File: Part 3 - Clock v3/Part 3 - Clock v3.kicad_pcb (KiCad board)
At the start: 2 copper layers, 100 x 100 mm, 88 parts, among them J1 BUS 1, J2 RST/CLK TP, J3 AUX PWR, SW1 RESET, SW2 MODE, SW3 SPEED, SW4 STEP, SW5 BOOT SPEED, SW6 BOOT MODE, SW7 SW_DIP_x08, SW8 RESET FAST LSB, SW9 RESET FAST MSB, U1 74AHC14, U10 74HC112, U11 74AHC74, U12 LMC555, U13 74HC251, U14 74HC40103, U15 74AHC138, U16 74HC251, U17 74HC251, U2 74AHC174, U3 74AHC08, U4 74AHC14, U5 74AHC74, U6 74AHC74, U7 74AHC74, U8 74AHC74, U9 74HC112, X1 14.7456MHz

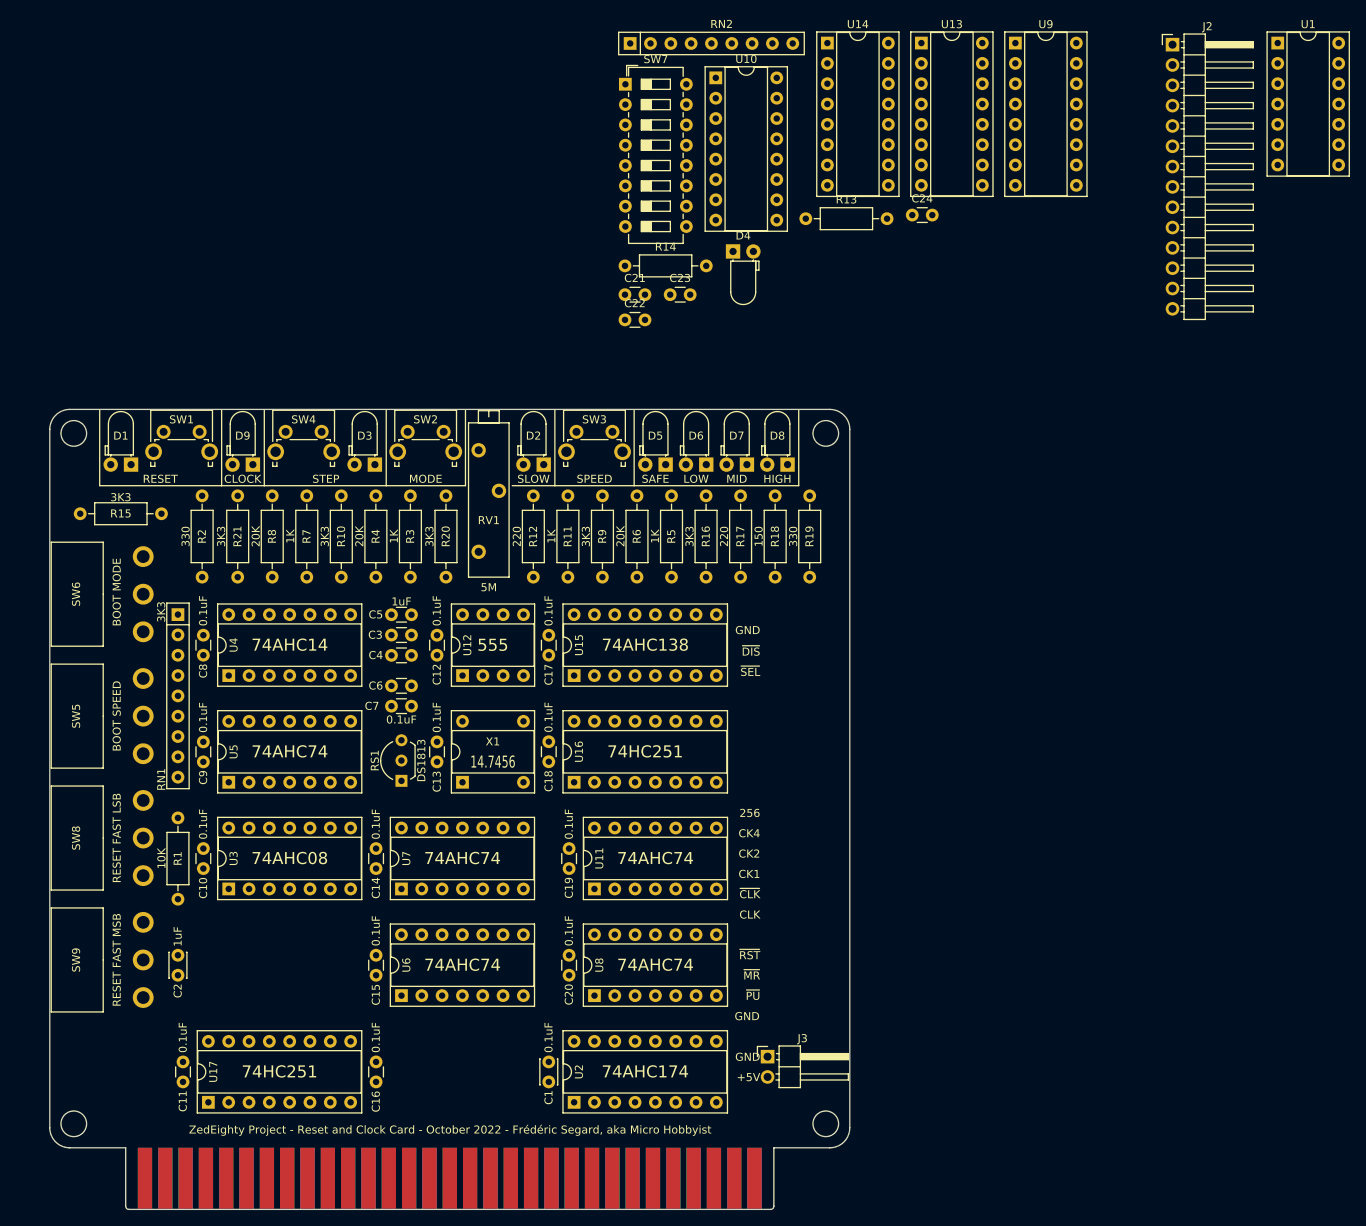
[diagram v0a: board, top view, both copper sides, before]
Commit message: Attempted to reduce chip count
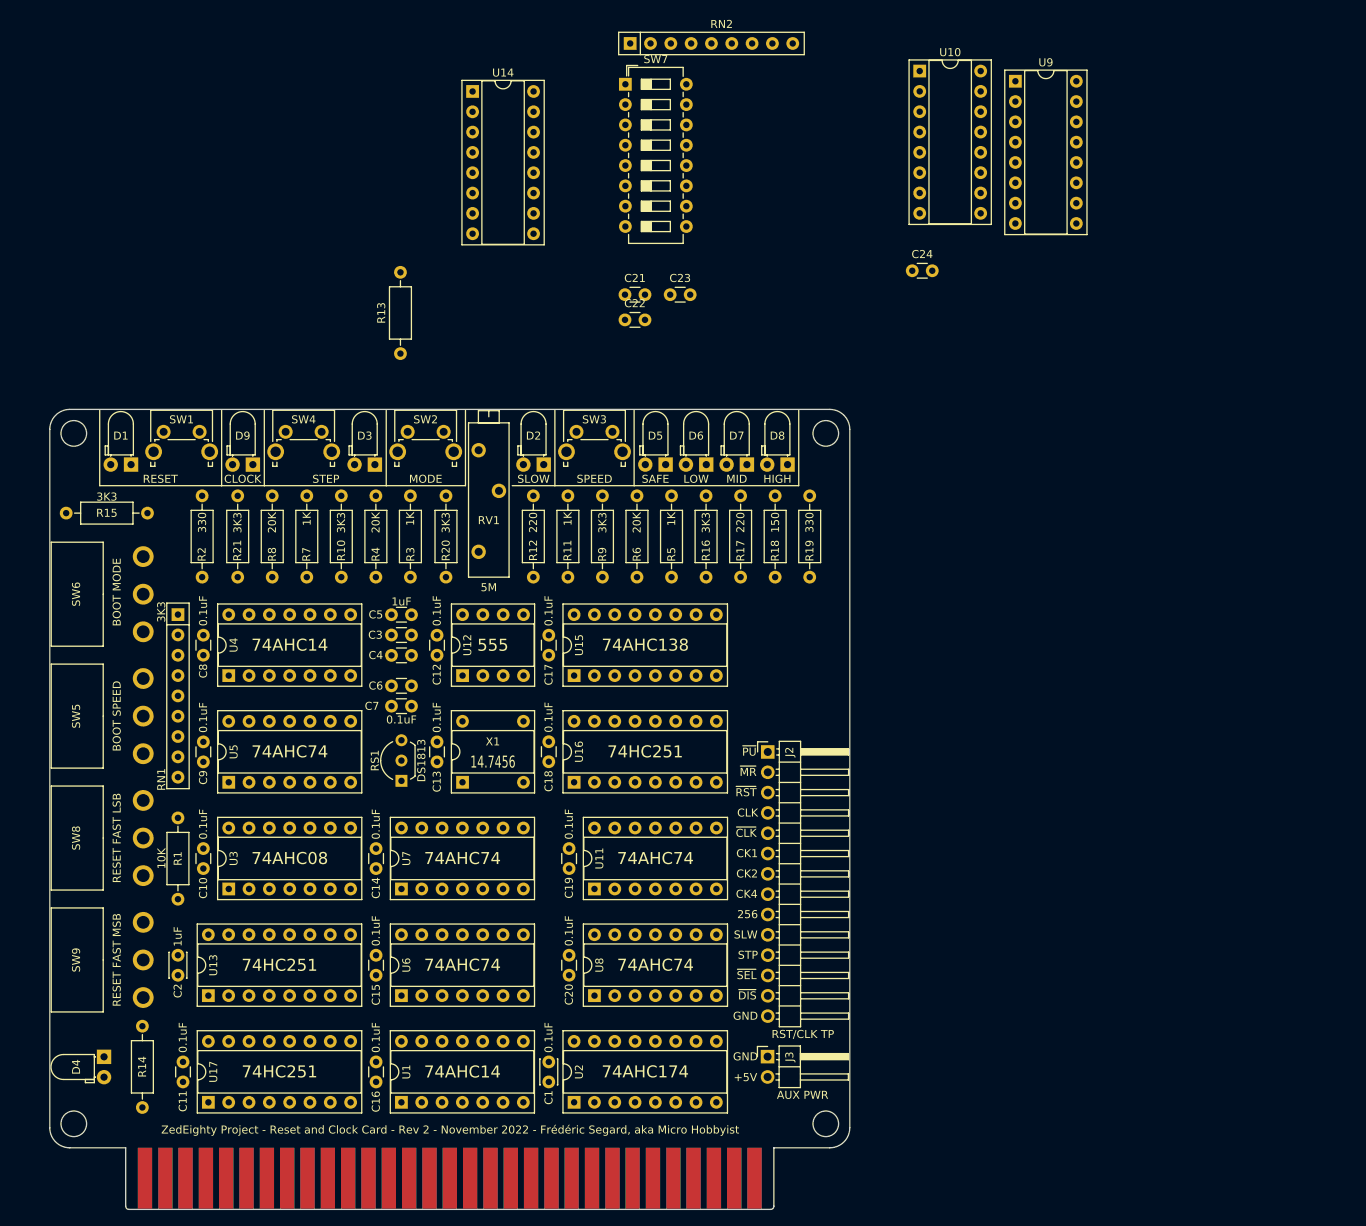
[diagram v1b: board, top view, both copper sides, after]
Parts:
- moved U1 171.8 mm to (133.3, 132.7), turned to 90 degrees
- moved U13 148.7 mm to (109.2, 119.4), turned to 90 degrees
- moved D4 127.7 mm to (96.2, 127.0), turned to -90 degrees
- moved R14 112.6 mm to (101.0, 123.2), turned to -90 degrees
- moved J2 101.9 mm to (179.1, 88.9)
- moved R13 53.4 mm to (133.2, 39.1), turned to 90 degrees
- moved U14 44.8 mm to (142.2, 6.35)
- moved U10 25.5 mm to (198.1, 3.80)
- moved C24 6.96 mm to (197.2, 28.8)
- moved U9 4.77 mm to (210.1, 5.07)
- moved R15 1.75 mm to (101.6, 59.1)
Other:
- board text added: "SLW"
- board text added: "STEP"
- board text added: "STP"
- board text added: "ZedEighty Project - Reset and Clock Card - Rev 2 - November 2022 - Frédéric Segard, aka Micro Hobbyist"
- board text added: "~{CLK} ~{DIS}"
- board text removed: "CLK DIS"
- board text removed: "ZedEighty Project - Reset and Clock Card - October 2022 - Frédéric Segard, aka Micro Hobbyist"

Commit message: Clock 3 and Keyboard
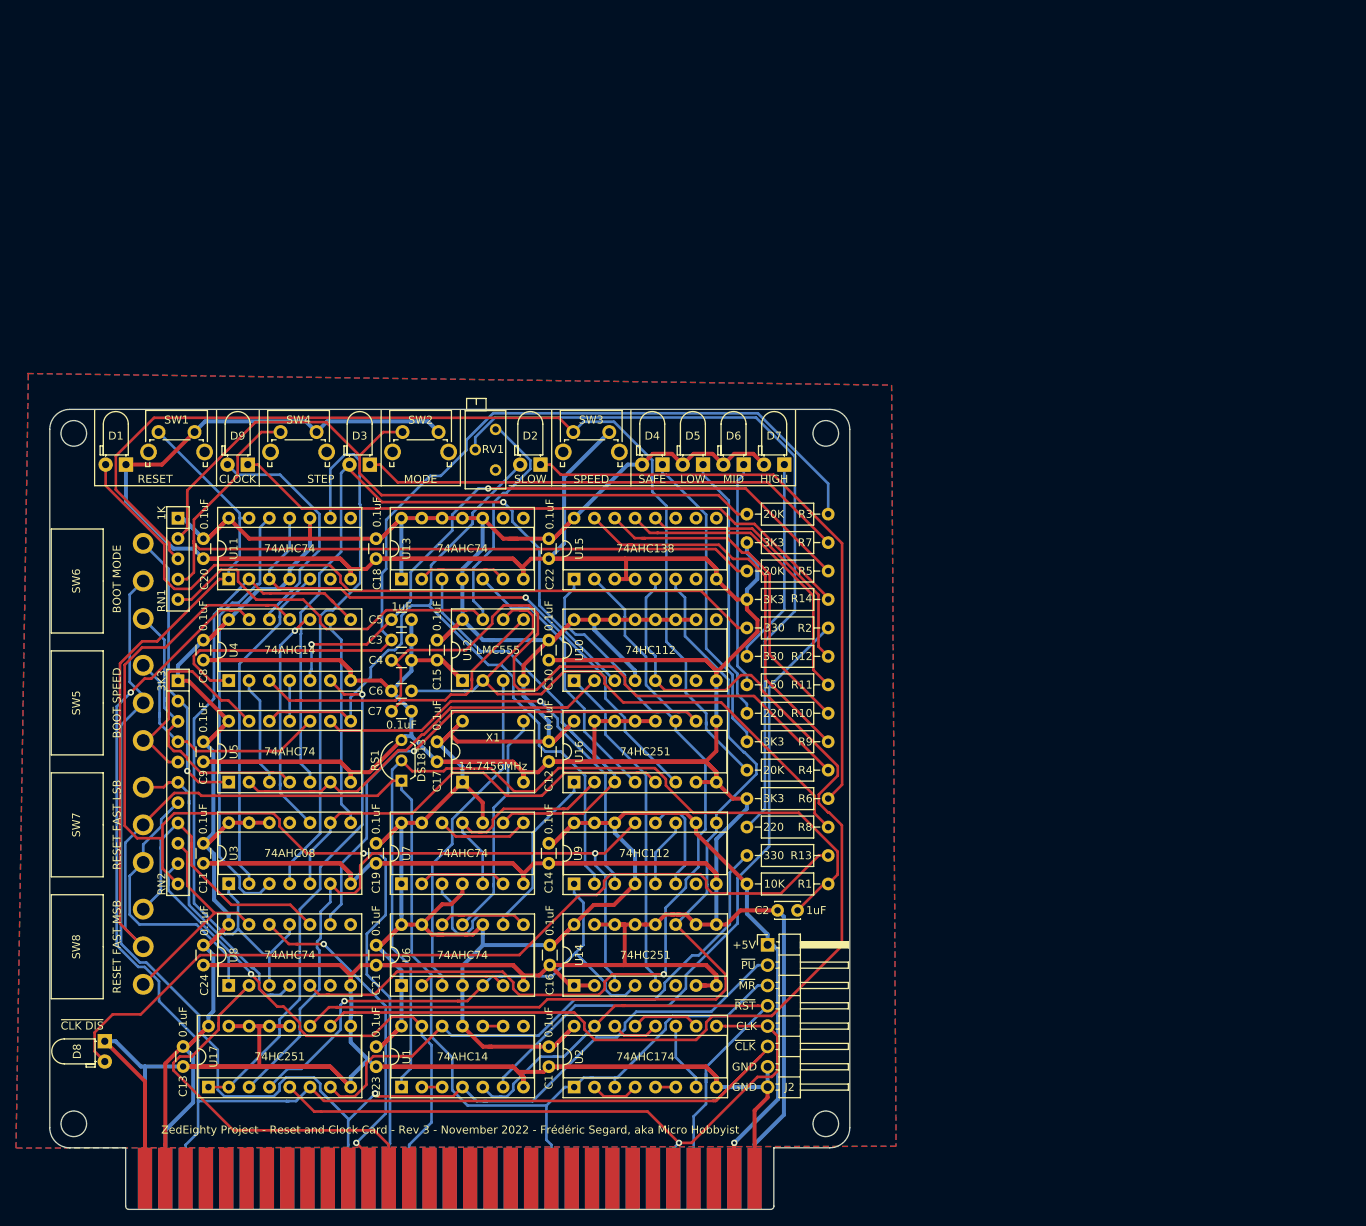
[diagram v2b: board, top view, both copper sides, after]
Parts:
- removed J3: AUX PWR, Connector_PinHeader_2.54mm:PinHeader_1x02_P2.54mm_Horizontal
- removed the R11 at (154.2, 67.1)
- removed the R13 at (133.2, 39.1)
- removed R15, R20: 3K3, Resistor_THT:R_Axial_DIN0207_L6.3mm_D2.5mm_P10.16mm_Horizontal
- removed the R3 at (134.5, 67.1)
- removed the R5 at (167.1, 67.1)
- removed the R7 at (121.5, 67.1)
- removed the SW7 at (161.3, 5.45)
- removed the U14 at (142.2, 6.35)
- added U13: 74AHC74, Package_DIP:DIP-14_W7.62mm_Socket, F.Cu at (133.3, 67.3)
- J2: footprint Connector_PinHeader_2.54mm:PinHeader_1x14_P2.54mm_Horizontal -> Connector_PinHeader_2.54mm:PinHeader_1x08_P2.54mm_Horizontal
- RN1: value 3K3 -> 1K; footprint Resistor_THT:R_Array_SIP9 -> Resistor_THT:R_Array_SIP5
- RN2: footprint Resistor_THT:R_Array_SIP9 -> Resistor_THT:R_Array_SIP11
- RV1: footprint Potentiometer_THT:Potentiometer_Bourns_3006P_Horizontal -> Potentiometer_THT:Potentiometer_Bourns_3296Z_Horizontal
- moved C24 122.3 mm to (108.6, 113.0), turned to -90 degrees
- moved U9 114.5 mm to (154.9, 105.4), turned to 90 degrees
- moved RN2 97.7 mm to (105.4, 80.0), turned to -90 degrees
- moved U10 87.6 mm to (154.9, 80.0), turned to 90 degrees
- moved R1 81.3 mm to (186.7, 105.4), turned to 180 degrees
- moved R13 78.5 mm to (176.5, 101.9), turned to 0 degrees
- moved R2 78.5 mm to (186.7, 73.4), turned to 180 degrees
- moved C2 77.7 mm to (182.9, 108.7), turned to 180 degrees
- moved R14 73.9 mm to (186.7, 69.8), turned to 180 degrees
- moved R5 69.5 mm to (186.7, 66.3), turned to 180 degrees
- moved R7 61.0 mm to (186.7, 62.7), turned to 180 degrees
- moved U11 59.9 mm to (111.8, 67.3)
- moved C20 59.4 mm to (108.6, 62.2), turned to -90 degrees
- moved R3 57.1 mm to (186.7, 59.2), turned to 180 degrees
- moved R8 49.3 mm to (176.5, 98.3), turned to 0 degrees
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- renumbered C17 to C10, C10 to C11, C18 to C12, C11 to C13, C19 to C14, C12 to C15, C20 to C16, C13 to C17, C21 to C18, C14 to C19, C22 to C20, C15 to C21, C23 to C22, C16 to C23, D5 to D4, D6 to D5, D7 to D6, D8 to D7, D4 to D8, R17 to R10, R18 to R11, R19 to R12, R14 to R13, R21 to R14, R4 to R3, R6 to R4, R8 to R5, R9 to R6, R10 to R7, R12 to R8, R16 to R9, SW8 to SW7, SW9 to SW8, U13 to U14
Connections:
- D2 pad 1: GND -> Net-(D2-Pad1)
- D3 pad 1: GND -> Net-(D3-Pad1)
- D9 pad 1: GND -> Net-(D9-Pad1)
- J2 pad 1: /~{PWR_UP} -> +5V
- J2 pad 2: /~{MR} -> /~{PWR_UP}
- J2 pad 3: /~{RESET} -> /~{MR}
- J2 pad 4: /CLK -> /~{RESET}
- J2 pad 5: /~{CLK} -> /CLK
- J2 pad 6: /CLK1 -> /~{CLK}
- J2 pad 7: /CLK2 -> GND
- J2 pad 8: /CLK4 -> GND
- R13 pad 1: Net-(R14-Pad1) -> Net-(R13-Pad1)
- R14 pad 1: Net-(R21-Pad1) -> Net-(D9-Pad1)
- R14 pad 2: Net-(D9-Pad2) -> GND
- R3 pad 2: Net-(R3-Pad2) -> /Clock/R3
- R4 pad 2: Net-(R5-Pad2) -> /Clock/R5
- R5 pad 2: Net-(R7-Pad2) -> /Clock/R7
- R6 pad 1: Net-(R9-Pad1) (its old number) -> Net-(D2-Pad1)
- R6 pad 2: Net-(D2-Pad2) -> GND
- R7 pad 1: Net-(R10-Pad1) (its old number) -> Net-(D3-Pad1)
- R7 pad 2: Net-(D3-Pad2) -> GND
- RN1 pad 2: /Clock/R13 -> /Clock/R3
- RN1 pad 3: /Clock/R10 -> /Clock/R5
- RN1 pad 4: /Clock/R9 -> /Clock/R7
- RN1 pad 5: /Clock/R12 -> /Clock/R11
- RN2 pad 1: GND -> +5V
- RN2 pad 2: Net-(RN2-Pad2) -> /Clock/R13
- RN2 pad 3: Net-(RN2-Pad3) -> /Clock/R10
- RN2 pad 4: Net-(RN2-Pad4) -> /Clock/R9
- RN2 pad 5: Net-(RN2-Pad5) -> /Clock/R12
- RN2 pad 6: Net-(RN2-Pad6) -> /Clock/R20
- RN2 pad 7: Net-(RN2-Pad7) -> /Clock/R24
- RN2 pad 8: Net-(RN2-Pad8) -> /Clock/R25
- RN2 pad 9: Net-(RN2-Pad9) -> /Clock/R21
- RV1 pad 3: Net-(R11-Pad2) -> /Clock/R11
- SW2 pad 1: Net-(R3-Pad2) -> /Clock/R3
- SW3 pad 1: Net-(R5-Pad2) -> /Clock/R5
- SW4 pad 1: Net-(R7-Pad2) -> /Clock/R7
- U1 pad 10: Net-(R14-Pad1) -> Net-(U1-Pad10)
- U1 pad 11: /~{CLK_DIS} -> +5V
- U1 pad 12: Net-(U1-Pad12) -> Net-(R13-Pad1)
- U1 pad 9: +5V -> Net-(U1-Pad10)
- U10 pad 3: Net-(R10-Pad1) (its old number) -> Net-(D3-Pad2)
- U12 pad 7: Net-(R11-Pad2) -> /Clock/R11
- U16 pad 1: /CLK1 -> /Clock/CLK1
- U16 pad 2: /CLK2 -> /Clock/CLK2
- U16 pad 3: /CLK4 -> /Clock/CLK4
- U16 pad 4: /CLK256 -> /Clock/CLK8
- U17 pad 7: Net-(U1-Pad12) -> Net-(R13-Pad1)
- U4 pad 12: Net-(R21-Pad1) -> Net-(D9-Pad2)
- U5 pad 12: Net-(R9-Pad1) (its old number) -> Net-(D2-Pad2)
- U5 pad 5: Net-(R10-Pad1) (its old number) -> Net-(D3-Pad2)
- U5 pad 8: Net-(R9-Pad1) (its old number) -> Net-(D2-Pad2)
- U6 pad 11: Net-(U12-Pad3) -> Net-(U6-Pad11)
- U6 pad 13: /~{PWR_UP} -> +5V
- U6 pad 3: /CLK1 -> Net-(U12-Pad3)
- U6 pad 5: /CLK2 -> /Clock/SLOW
- U6 pad 9: /Clock/SLOW -> /Clock/CLK1
- U7 pad 11: /CLK2 -> /Clock/CLK2
- U7 pad 3: /OSC -> /Clock/CLK1
- U7 pad 5: /CLK1 -> /Clock/CLK2
- U7 pad 9: /CLK4 -> /Clock/CLK4
- U9 pad 2: Net-(R9-Pad1) (its old number) -> Net-(D2-Pad2)
- X1 pad 5: /OSC -> Net-(U6-Pad11)
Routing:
- net GND: track 0.00 -> 1112.9 mm
- net +5V: track 0.00 -> 621.0 mm, vias 0 -> 1
- net /~{MR}: track 0.00 -> 230.0 mm
- net /~{CLK}: track 0.00 -> 170.9 mm, vias 0 -> 1
- net /~{PWR_UP}: track 0.00 -> 163.2 mm, vias 0 -> 1
- net /Clock/STEP/~{RUN}: track 0.00 -> 140.2 mm
- net /Clock/R5: track 0.00 -> 132.3 mm
- net /~{CLK_SEL}: track 0.00 -> 131.9 mm, vias 0 -> 1
- net /Clock/FAST/~{SLOW}: track 0.00 -> 116.8 mm
- net Net-(C3-Pad1): track 0.00 -> 116.4 mm
- net Net-(C2-Pad1): track 0.00 -> 114.9 mm
- net /Clock/Q0: track 0.00 -> 111.4 mm, vias 0 -> 1
- net Net-(D8-Pad2): track 0.00 -> 108.0 mm
- net Net-(C4-Pad1): track 0.00 -> 101.7 mm
- net Net-(D2-Pad2): track 0.00 -> 99.6 mm
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- added copper zone on B.Cu, net GND
- added copper zone on F.Cu, net GND
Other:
- board text added: "921K"
- board text added: "< SLOW >"
- board text added: "ZedEighty Project - Reset and Clock Card - Rev 3 - November 2022 - Frédéric Segard, aka Micro Hobbyist"
- board text removed: "-- SLOW --"
- board text removed: "1.8432"
- board text removed: "14.7456"
- board text removed: "256"
- board text removed: "3.6864"
- board text removed: "460K"
- board text removed: "555"
- board text removed: "7.3728"
- board text removed: "CK1"
- board text removed: "CK2"
- board text removed: "CK4"
- board text removed: "DIVCLK"
- board text removed: "SLW"
- board text removed: "STEP"
- board text removed: "STP"
- board text removed: "ZedEighty Project - Reset and Clock Card - Rev 2 - November 2022 - Frédéric Segard, aka Micro Hobbyist"
- board text removed: "~{CLK_DIS}"
- board text removed: "~{CLK_SEL}"
- board text removed: "~{DIS}"
- board text removed: "~{PWR_UP}"
- board text removed: "~{RESET}"
- board text removed: "~{SEL}"

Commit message: Added Keyboard, and minor fixes
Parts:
- U1, U4: value 74AHC14 -> 74AC14
- U10, U9: value 74HC112 -> 74AC112
- U11, U13, U5, U6, U7, U8: value 74AHC74 -> 74AC74
- U15: value 74AHC138 -> 74HC138
- U2: value 74AHC174 -> 74AC174
- U3: value 74AHC08 -> 74AC08
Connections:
- net /~{IORD} renamed /USER5
- net /~{IOWR} renamed /USER6
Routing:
- net /Clock/CLK4: track 62.0 -> 52.4 mm
- net /~{CLK}: track 170.9 -> 162.0 mm
- net +5V: track 621.0 -> 614.2 mm
- net Net-(D9-Pad2): track 33.1 -> 29.8 mm
- net /~{RESET}: track 68.8 -> 66.7 mm
- net Net-(C6-Pad1): track 81.4 -> 79.5 mm
- net Net-(U10-Pad2): track 51.7 -> 50.4 mm
- net Net-(U3-Pad10): track 30.1 -> 28.8 mm
- net /Clock/Q0: track 111.4 -> 110.2 mm
- net /Clock/R10: track 36.4 -> 35.3 mm
- net Net-(U2-Pad12): track 7.05 -> 6.05 mm
- net Net-(U13-Pad2): track 12.1 -> 11.1 mm
- net Net-(R13-Pad1): track 72.8 -> 71.9 mm
- net /Clock/SLOW: track 68.1 -> 67.2 mm
- net Net-(U6-Pad12): track 12.0 -> 11.1 mm
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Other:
- board text added: "10K"
- board text added: "20K"
- board text added: "220"
- board text added: "330"
- board text added: "3K3"
- board text added: "555"
- board text added: "74AC08"
- board text added: "74AC112"
- board text added: "74AC14"
- board text added: "74AC174"
- board text added: "74AC74"
- board text added: "74HC138"
- board text added: "74HC251"
- board text added: "MODE"
- board text added: "RESET"
- board text added: "SPEED"
- board text added: "STEP"
- board text added: "XTAL"
- board text added: "ZedEighty Project - Reset and Clock Card - Rev 3 - Frédéric Segard, youtube.com/@microhobbyist"
- board text added: "~{CLK_DIS}"
- board text added: "~{PWR_UP}"
- board text added: "~{RESET}"
- board text removed: "--- RESET ---"
- board text removed: "---- STEP ----"
- board text removed: "------ FAST ------"
- board text removed: "< MODE >"
- board text removed: "< SLOW >"
- board text removed: "< SPEED >"
- board text removed: "ZedEighty Project - Reset and Clock Card - Rev 3 - November 2022 - Frédéric Segard, aka Micro Hobbyist"
- board text removed: "~{CLK} ~{DIS}"

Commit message: Updated key library and keyboard
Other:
- rule pad_to_mask_clearance: 0 -> 0.2
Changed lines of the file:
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@@
       (dielectric_constraints no)
     )
-    (pad_to_mask_clearance 0)
+    (pad_to_mask_clearance 0.2)
+    (solder_mask_min_width 0.05)
     (pcbplotparams
       (layerselection 0x00010fc_ffffffff)
@@
       (psa4output false)
       (plotreference true)
-      (plotvalue false)
+      (plotvalue true)
       (plotinvisibletext false)
       (sketchpadsonfab false)
@@
       (drillshape 0)
       (scaleselection 1)
-      (outputdirectory "Gerber")
+      (outputdirectory "Gerber/")
     )
   )
